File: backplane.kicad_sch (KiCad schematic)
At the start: 6 parts, among them J5 XT60PW-F

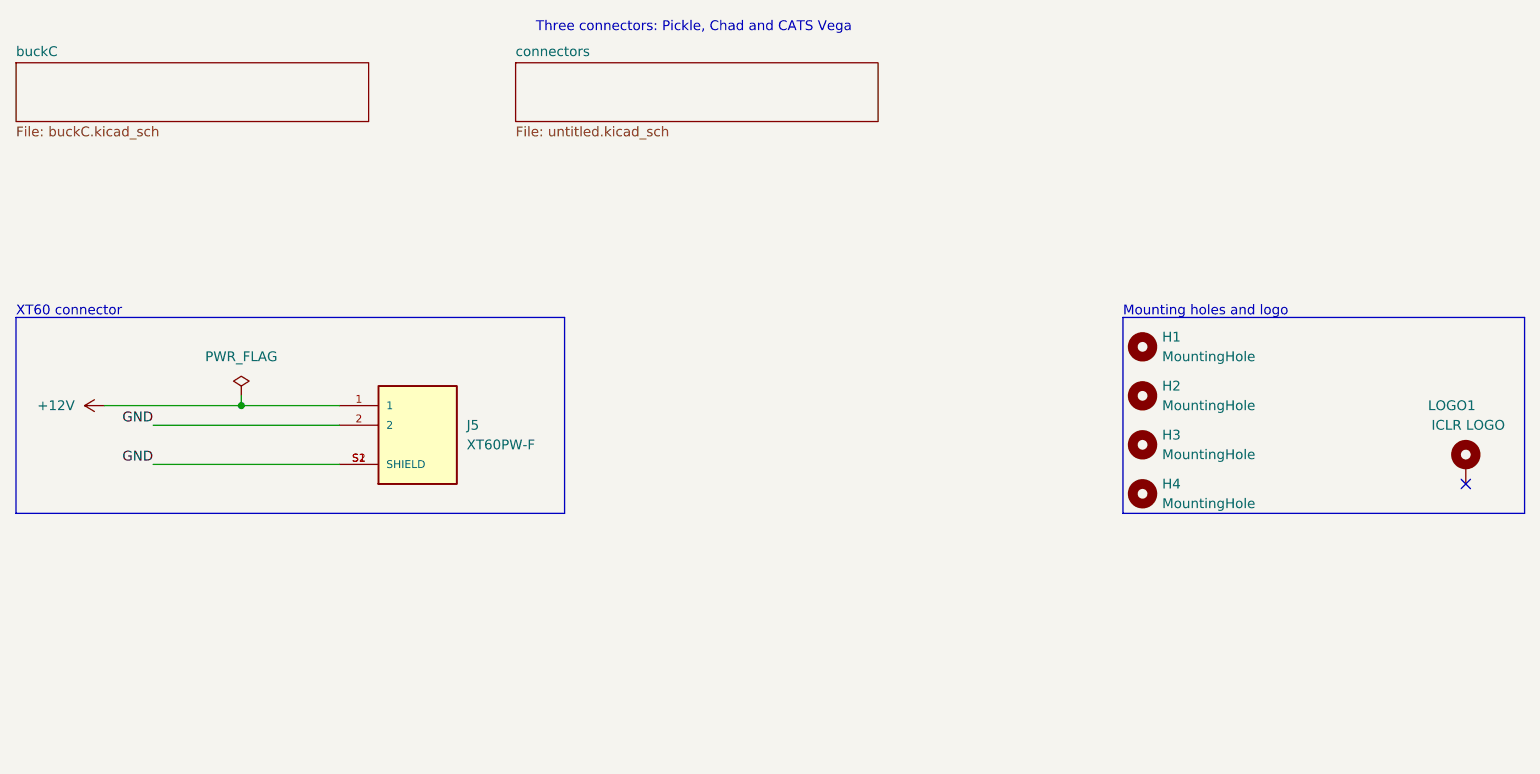
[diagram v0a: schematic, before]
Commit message: neatened things
leds
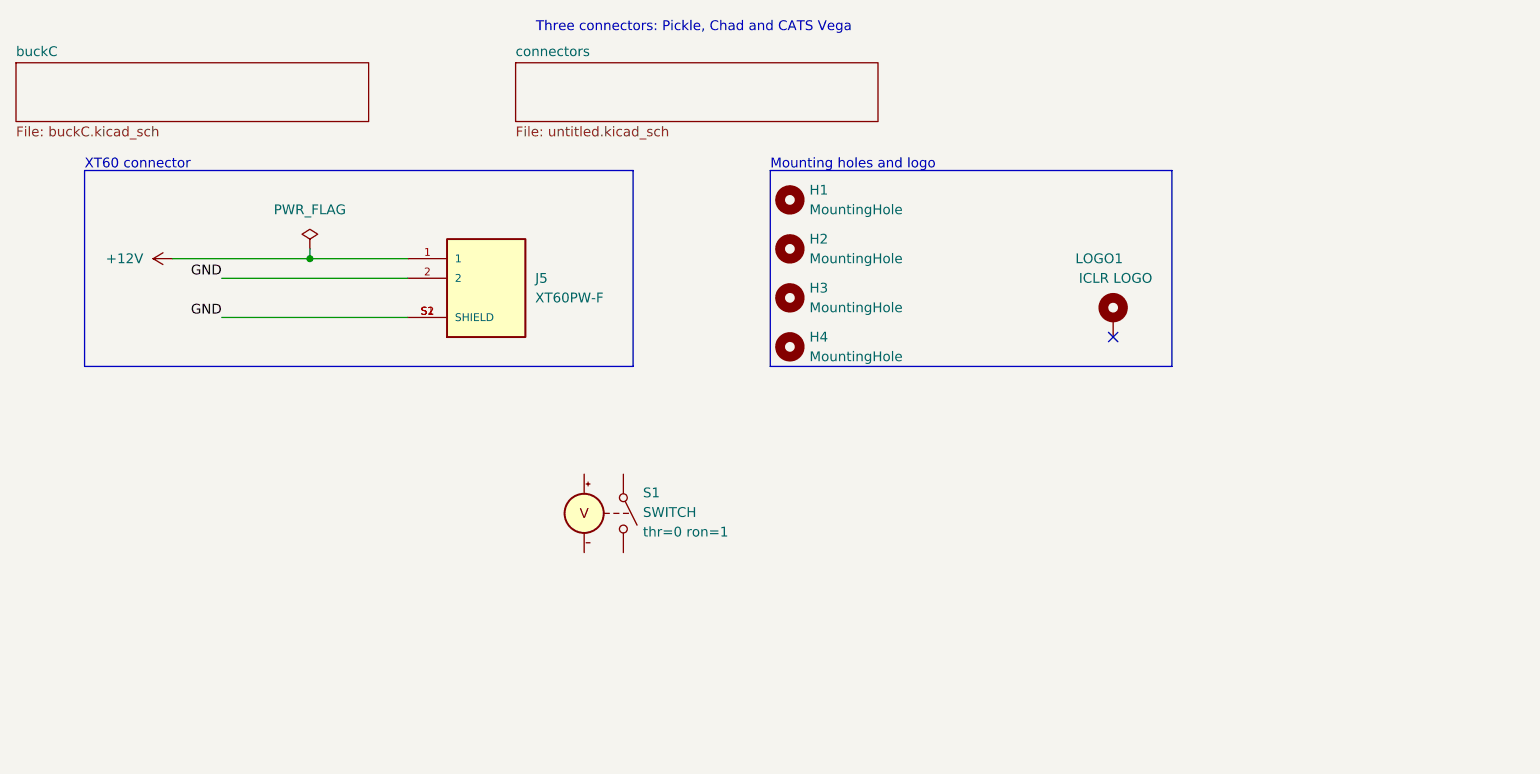
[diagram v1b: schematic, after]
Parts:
- added S1: SWITCH, symbol Simulation_SPICE:SWITCH
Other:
- moved on the sheet: H1, H2, H3, H4, J5, LOGO1

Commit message: reducing more DRCs
zone violations etc
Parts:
- removed S1: SWITCH, symbol Simulation_SPICE:SWITCH
- added 12VLED1, 12VLED2: 12VLED, LED_SMD:LED_0402_1005Metric, symbol Device:LED_Small
- added 3.3VLED1, 3.3VLED2: 3.3VLED, LED_SMD:LED_0402_1005Metric, symbol Device:LED_Small
- added R1, R2, R7, R8: 1k, Resistor_SMD:R_0402_1005Metric, symbol Device:R_Small
- added TP1, TP2, TP3, TP4: TestPoint, TestPoint:TestPoint_Pad_D1.0mm, symbol Connector:TestPoint
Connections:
- net +12V: now also 12VLED1.2 (A), 12VLED2.2 (A), TP2.1, TP4.1
- net GND: now also R1.1, R2.1, R7.1, R8.1
- new net: 3.3VLED1.1 (K), R1.2
- new net: 3.3VLED2.1 (K), R2.2
- new net: 12VLED1.1 (K), R8.2
- new net: 12VLED2.1 (K), R7.2
- new net +3.3V: 3.3VLED1.2 (A), 3.3VLED2.2 (A), TP1.1, TP3.1
